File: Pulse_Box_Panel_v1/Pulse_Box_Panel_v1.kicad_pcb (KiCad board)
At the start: 2 copper layers, 80 x 80 mm, 44 parts, among them J1 Conn_01x11, J2 Conn_01x11, J3 Conn_01x11, J4 Conn_01x11, J5 Conn_01x03, J6 Conn_01x03, J7 Conn_02x05_Odd_Even, J8 Conn_01x03, J9 Conn_01x04_Pin, U1 STM32G0B1CBTx, U2 74HCT4051, U3 74HCT4051, U4 TPS54560BDDA, U5 AP2112K-3.3, Y1 8MHz Crystal

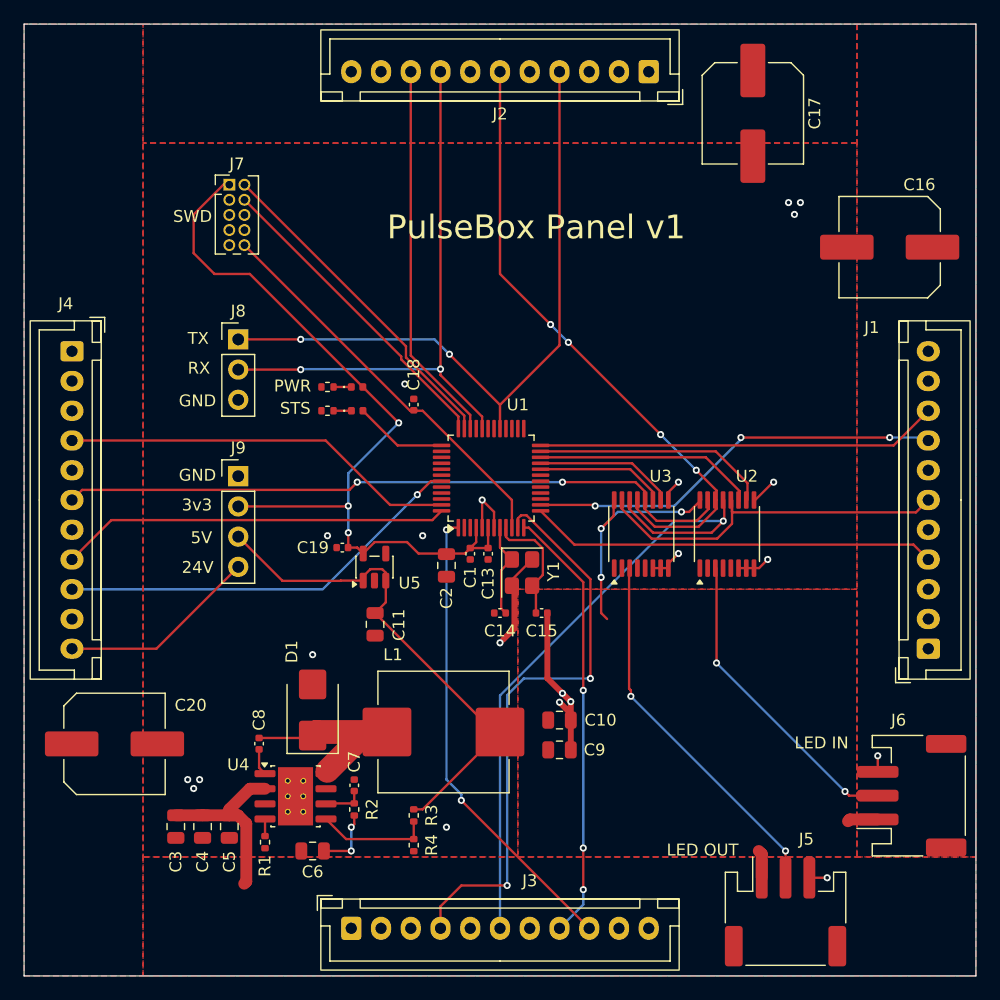
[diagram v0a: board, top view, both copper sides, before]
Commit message: complete v2 and v1 panel design, this is the final design sent to jlcpcb for v2
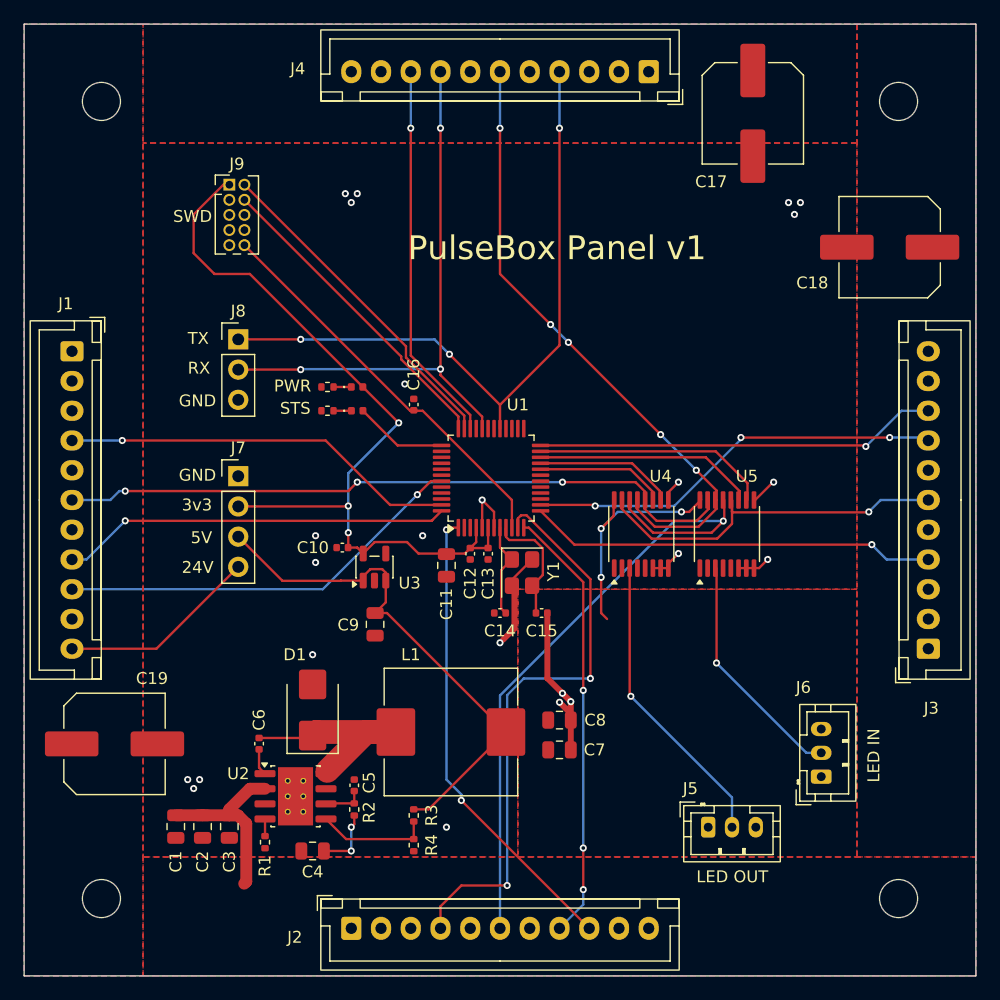
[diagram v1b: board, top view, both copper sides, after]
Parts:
- added H1: MountingHole, MountingHole:MountingHole_3.2mm_M3, F.Cu at (156.5, 56.5)
- added H2: MountingHole, MountingHole:MountingHole_3.2mm_M3, F.Cu at (223.5, 56.5)
- added H3: MountingHole, MountingHole:MountingHole_3.2mm_M3, F.Cu at (223.5, 123.5)
- added H4: MountingHole, MountingHole:MountingHole_3.2mm_M3, F.Cu at (156.5, 123.5)
- J5, J6: footprint Connector_JST:JST_PH_S3B-PH-SM4-TB_1x03-1MP_P2.00mm_Horizontal -> Connector_JST:JST_PH_B3B-PH-K_1x03_P2.00mm_Vertical
- L1: footprint Inductor_SMD:L_APV_APH1030 -> Inductor_SMD:L_TechFuse_SL1040
- moved J5 9.63 mm to (207.5, 117.5)
- moved J6 7.77 mm to (217.0, 113.2)
- moved L1 0.62 mm to (185.9, 109.5)
- renumbered C3 to C1, C19 to C10, C2 to C11, C1 to C12, C18 to C16, C16 to C18, C20 to C19, C4 to C2, C5 to C3, C6 to C4, C7 to C5, C8 to C6, C9 to C7, C10 to C8, C11 to C9, J4 to J1, J3 to J2, J1 to J3, J2 to J4, J9 to J7, J7 to J9, U4 to U2, U5 to U3, U3 to U4, U2 to U5
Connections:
- J1 pad 6: W_LED_PWM -> E_LED_PWM
- J3 pad 6: E_LED_PWM -> W_LED_PWM
- U4 pad 12: W_LED_PWM -> E_LED_PWM
- U4 pad 15: E_LED_PWM -> W_LED_PWM
- U5 pad 12: E_LED_PWM -> W_LED_PWM
- U5 pad 15: W_LED_PWM -> E_LED_PWM
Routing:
- net E_LED_PWM: track 31.5 -> 57.5 mm, vias 0 -> 3
- net W_LED_PWM: track 57.5 -> 31.5 mm, vias 2 -> 1
- net PWM_5V: track 26.1 -> 19.9 mm, vias 2 -> 1
- net PWM_DOUT: track 31.5 -> 25.3 mm, vias 2 -> 1
- net +5V: track 68.4 -> 65.0 mm
- net GND: track 42.8 -> 39.9 mm, vias 22 -> 24
- net Net-(D1-K): track 17.3 -> 18.8 mm
- net E_SENSE: track 33.8 -> 33.9 mm, vias 0 -> 1
- net UART3_RX: vias 0 -> 1
- net UART2_TX: vias 0 -> 1
- net UART1_RX: vias 2 -> 3
- net UART3_TX: vias 0 -> 1
- net UART1_TX: vias 2 -> 3
- net N_SENSE: vias 0 -> 1
- net N_LED_PWM: vias 4 -> 5

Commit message: basic readme with board summaries
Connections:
- J1 pad 9: W_SENSE -> E_SENSE
- J3 pad 9: E_SENSE -> W_SENSE
- U1 pad 24: E_SENSE -> W_SENSE
- U1 pad 43: W_SENSE -> E_SENSE
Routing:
- net W_SENSE: track 34.8 -> 33.9 mm
- net E_SENSE: track 33.9 -> 34.8 mm
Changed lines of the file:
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@@
 			(layers "F.Cu" "F.Mask" "F.Paste")
 			(roundrect_rratio 0.25)
-			(net 10 "E_SENSE")
+			(net 30 "W_SENSE")
 			(pinfunction "PB12")
 			(pintype "bidirectional")
@@
 			(layers "F.Cu" "F.Mask" "F.Paste")
 			(roundrect_rratio 0.25)
-			(net 30 "W_SENSE")
+			(net 10 "E_SENSE")
 			(pinfunction "PB4")
 			(pintype "bidirectional")
@@
 			(layers "*.Cu" "*.Mask")
 			(remove_unused_layers no)
-			(net 10 "E_SENSE")
+			(net 30 "W_SENSE")
 			(pinfunction "Pin_9")
 			(pintype "passive")
@@
 			(layers "*.Cu" "*.Mask")
 			(remove_unused_layers no)
-			(net 30 "W_SENSE")
+			(net 10 "E_SENSE")
 			(pinfunction "Pin_9")
 			(pintype "passive")
@@
 	)
 	(segment
-		(start 220.6625 85.4125)
-		(end 220.75 85.5)
+		(start 183.05 89.55)
+		(end 184.1875 88.4125)
 		(width 0.2)
 		(layer "F.Cu")
@@
 	)
 	(segment
-		(start 193.4125 85.4125)
-		(end 220.6625 85.4125)
+		(start 184.1875 88.4125)
+		(end 185.0875 88.4125)
 		(width 0.2)
 		(layer "F.Cu")
@@
 	)
 	(via
-		(at 220.75 85.5)
+		(at 183.05 89.55)
 		(size 0.6)
 		(drill 0.3)
@@
 	)
 	(segment
-		(start 220.75 85.5)
-		(end 223.75 82.5)
+		(start 175.1 97.5)
+		(end 154.025 97.5)
 		(width 0.2)
 		(layer "B.Cu")
@@
 	)
 	(segment
-		(start 223.75 82.5)
-		(end 226 82.5)
+		(start 183.05 89.55)
+		(end 175.1 97.5)
 		(width 0.2)
 		(layer "B.Cu")
@@
 	)
 	(segment
-		(start 183.05 89.55)
-		(end 184.1875 88.4125)
+		(start 220.6625 85.4125)
+		(end 220.75 85.5)
 		(width 0.2)
 		(layer "F.Cu")
@@
 	)
 	(segment
-		(start 184.1875 88.4125)
-		(end 185.0875 88.4125)
+		(start 193.4125 85.4125)
+		(end 220.6625 85.4125)
 		(width 0.2)
 		(layer "F.Cu")
@@
 	)
 	(via
-		(at 183.05 89.55)
+		(at 220.75 85.5)
 		(size 0.6)
 		(drill 0.3)
@@
 	)
 	(segment
-		(start 175.1 97.5)
-		(end 154.025 97.5)
+		(start 220.75 85.5)
+		(end 223.75 82.5)
 		(width 0.2)
 		(layer "B.Cu")
@@
 	)
 	(segment
-		(start 183.05 89.55)
-		(end 175.1 97.5)
+		(start 223.75 82.5)
+		(end 226 82.5)
 		(width 0.2)
 		(layer "B.Cu")
